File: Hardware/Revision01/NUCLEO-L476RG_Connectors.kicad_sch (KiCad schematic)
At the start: 29 parts, among them CN1 Header 19X2, CN2 Header 8X1_Female, CN3 Header 6X1_Female, CN4 Header 10X1_Female, CN5 Header 8X1_Female, CN6 Header 19X2

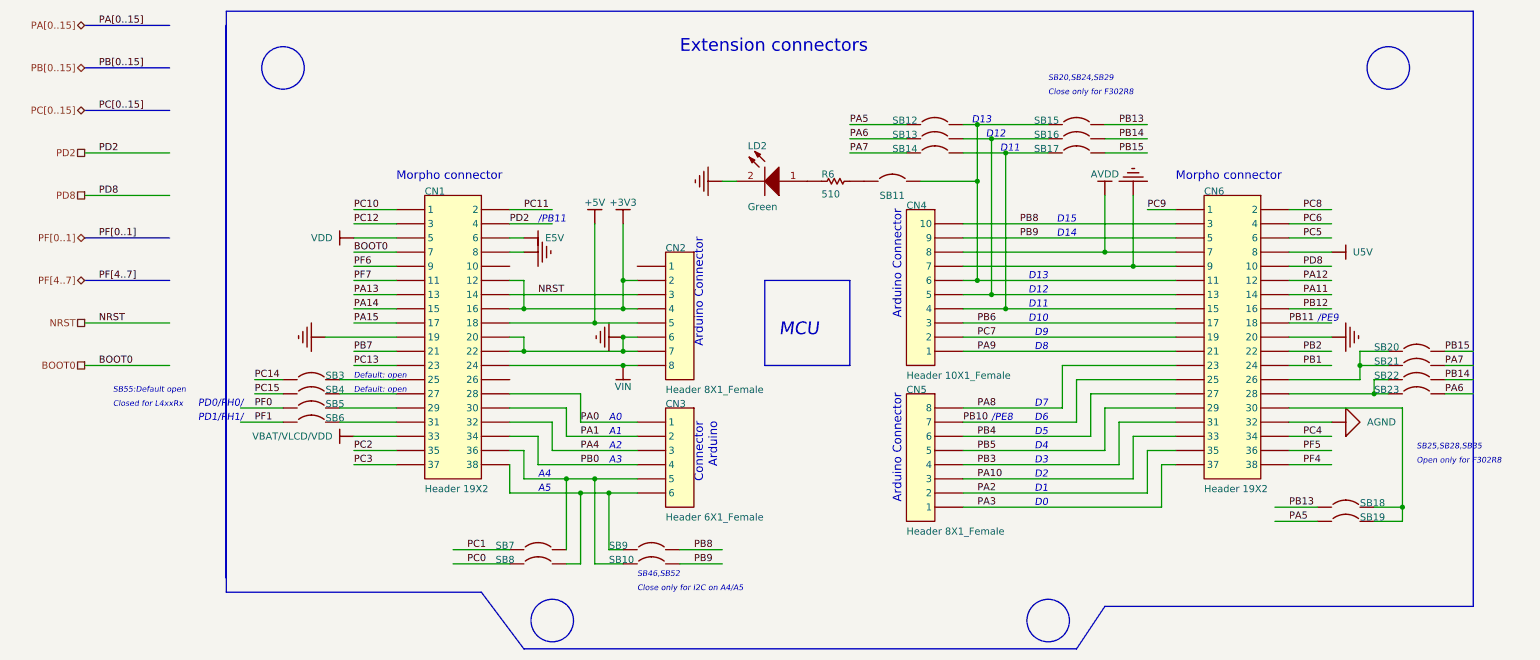
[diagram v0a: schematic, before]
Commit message: . Renamed schematic files, removed old symbol files
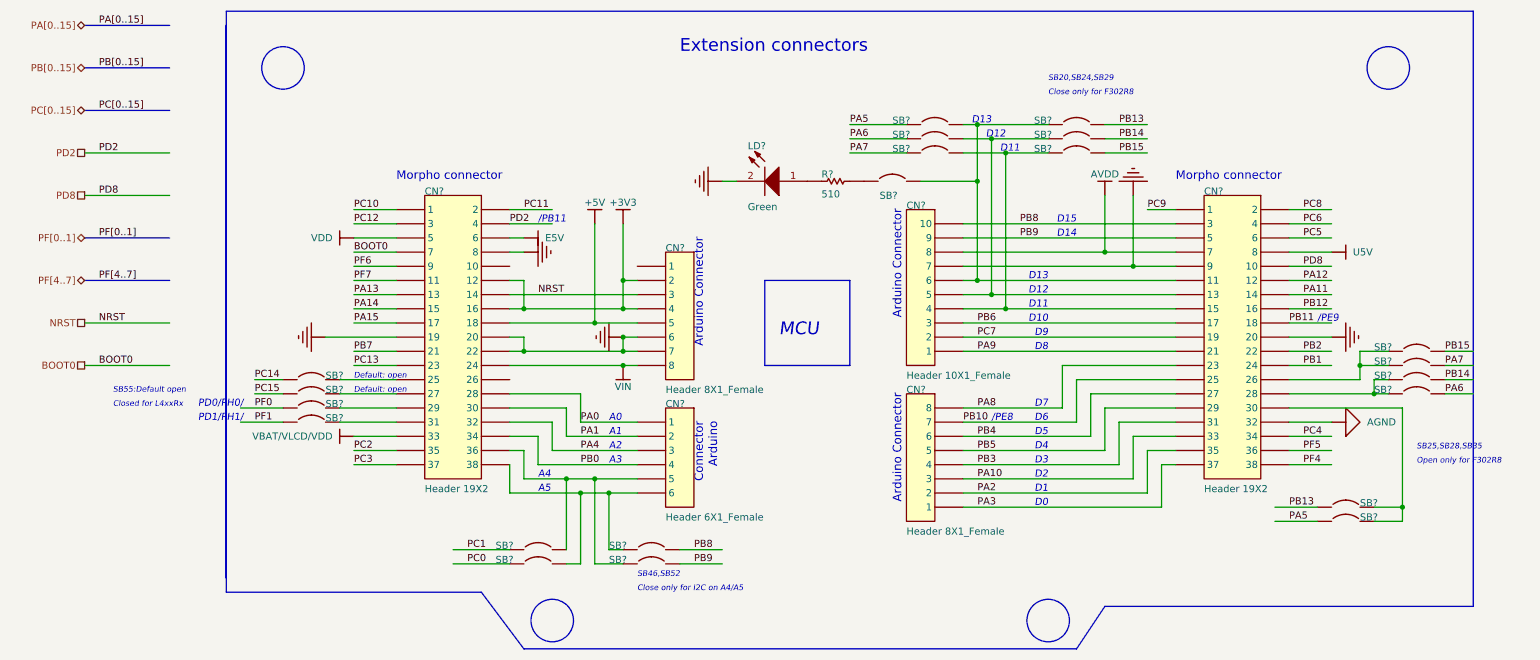
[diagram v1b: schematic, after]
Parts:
- renumbered CN4 to CN?, CN6 to CN?, CN5 to CN?, CN1 to CN?, CN3 to CN?, CN2 to CN?, LD2 to LD?, R6 to R?, SB21 to SB?, SB22 to SB?, SB16 to SB?, SB8 to SB?, SB20 to SB?, SB17 to SB?, SB5 to SB?, SB13 to SB?, SB14 to SB?, SB12 to SB?, SB4 to SB?, SB11 to SB?, SB15 to SB?, SB9 to SB?, SB10 to SB?, SB23 to SB?, SB18 to SB?, SB3 to SB?, SB19 to SB?, SB6 to SB?, SB7 to SB?

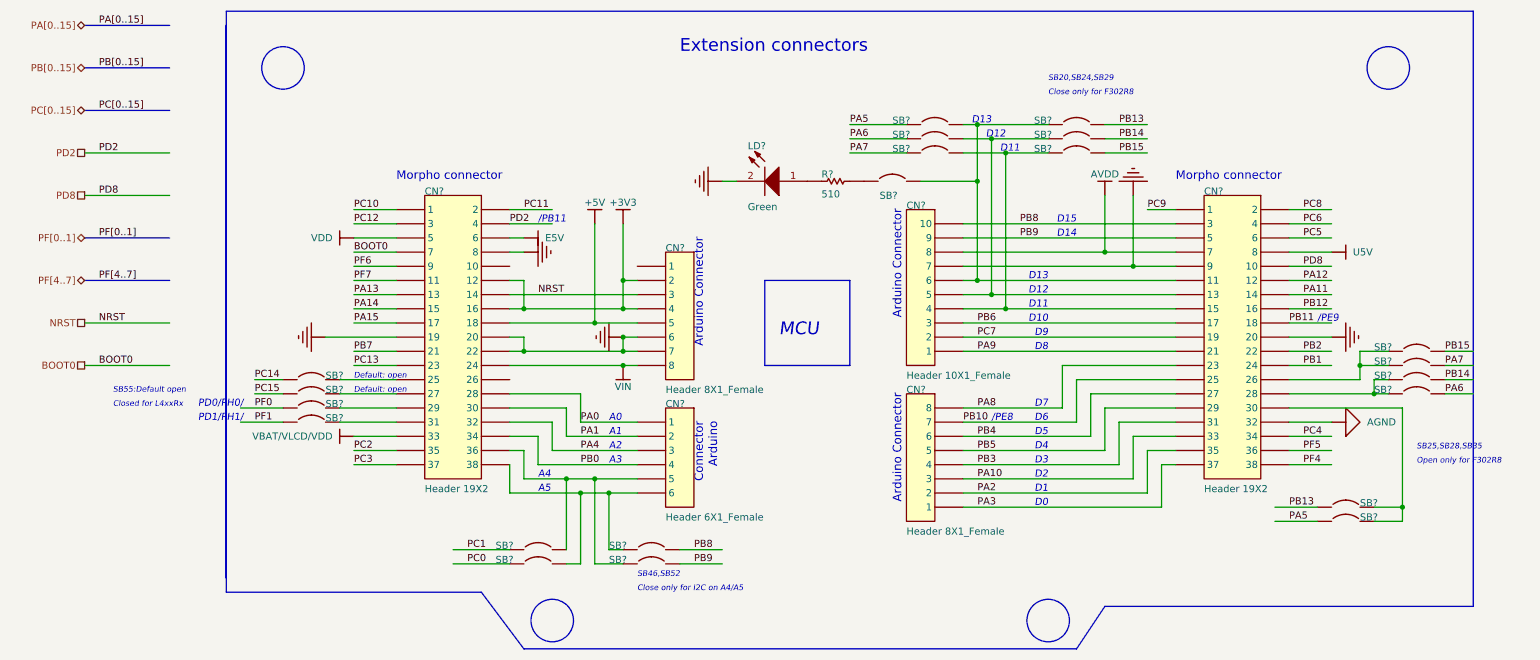
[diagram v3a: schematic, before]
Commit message: . Completed MCU schematic & imported hierarchical model pins
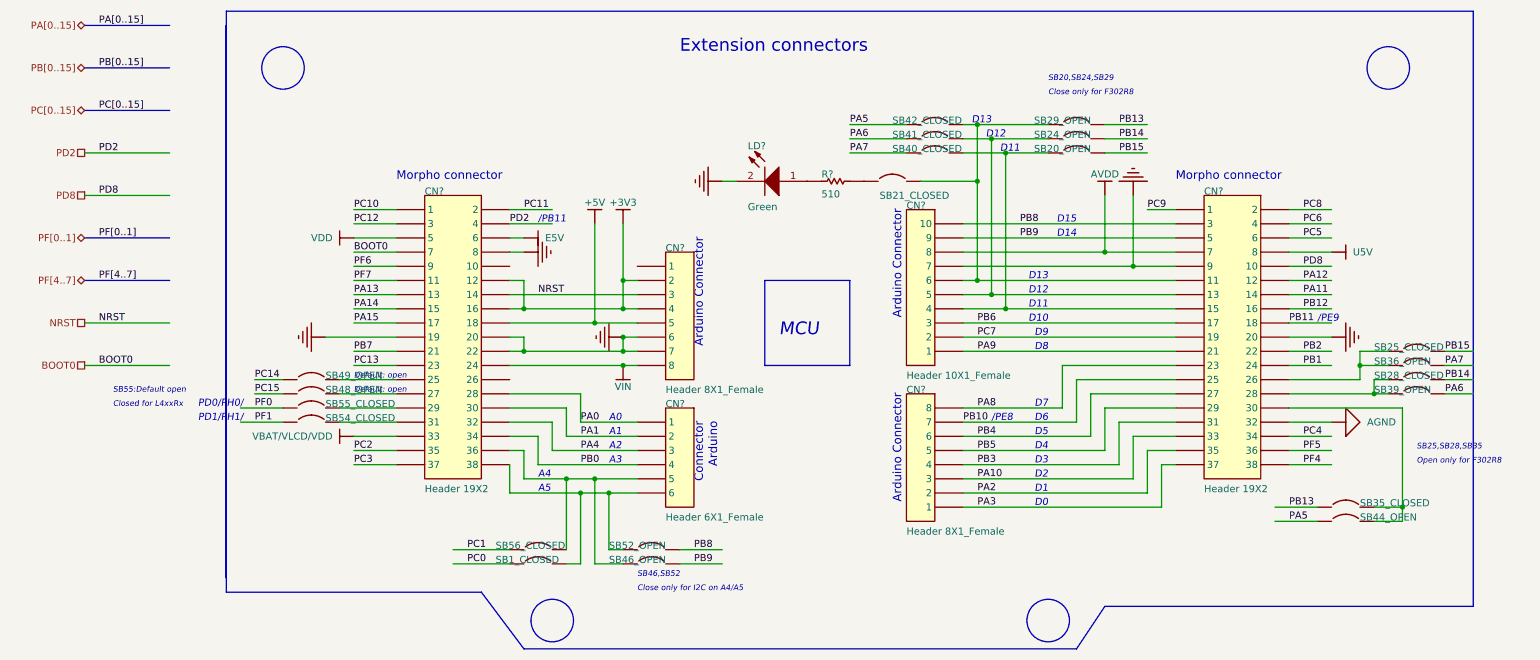
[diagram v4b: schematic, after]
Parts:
- gave numbers to parts that had none: 21
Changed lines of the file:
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@@
 		(on_board yes)
 		(dnp no)
-		(property "Reference" "SB?"
+		(property "Reference" "SB36_OPEN"
 			(at 257.81 95.25 0)
 			(effects
@@
 			(project "Revision01"
 				(path "/955cc99e-a129-42cf-abc7-aa99813fdb5f/00000000-0000-0000-0000-00005ea70ac3/dfd3e576-45ac-414e-879c-fe3a4e293d3a/d95c2c22-4412-4afc-9129-04f7fbe3da60"
-					(reference "SB?")
+					(reference "SB36_OPEN")
 					(unit 1)
 				)
@@
 		(on_board yes)
 		(dnp no)
-		(property "Reference" "SB?"
+		(property "Reference" "SB28_CLOSED"
 			(at 257.81 97.79 0)
 			(effects
@@
 			(project "Revision01"
 				(path "/955cc99e-a129-42cf-abc7-aa99813fdb5f/00000000-0000-0000-0000-00005ea70ac3/dfd3e576-45ac-414e-879c-fe3a4e293d3a/d95c2c22-4412-4afc-9129-04f7fbe3da60"
-					(reference "SB?")
+					(reference "SB28_CLOSED")
 					(unit 1)
 				)
@@
 		(on_board yes)
 		(dnp no)
-		(property "Reference" "SB?"
+		(property "Reference" "SB24_OPEN"
 			(at 196.85 54.61 0)
 			(effects
@@
 			(project "Revision01"
 				(path "/955cc99e-a129-42cf-abc7-aa99813fdb5f/00000000-0000-0000-0000-00005ea70ac3/dfd3e576-45ac-414e-879c-fe3a4e293d3a/d95c2c22-4412-4afc-9129-04f7fbe3da60"
-					(reference "SB?")
+					(reference "SB24_OPEN")
 					(unit 1)
 				)
@@
 		(on_board yes)
 		(dnp no)
-		(property "Reference" "SB?"
+		(property "Reference" "SB1_CLOSED"
 			(at 100.33 130.81 0)
 			(effects
@@
 			(project "Revision01"
 				(path "/955cc99e-a129-42cf-abc7-aa99813fdb5f/00000000-0000-0000-0000-00005ea70ac3/dfd3e576-45ac-414e-879c-fe3a4e293d3a/d95c2c22-4412-4afc-9129-04f7fbe3da60"
-					(reference "SB?")
+					(reference "SB1_CLOSED")
 					(unit 1)
 				)
@@
 		(on_board yes)
 		(dnp no)
-		(property "Reference" "SB?"
+		(property "Reference" "SB25_CLOSED"
 			(at 257.81 92.71 0)
 			(effects
@@
 			(project "Revision01"
 				(path "/955cc99e-a129-42cf-abc7-aa99813fdb5f/00000000-0000-0000-0000-00005ea70ac3/dfd3e576-45ac-414e-879c-fe3a4e293d3a/d95c2c22-4412-4afc-9129-04f7fbe3da60"
-					(reference "SB?")
+					(reference "SB25_CLOSED")
 					(unit 1)
 				)
@@
 		(on_board yes)
 		(dnp no)
-		(property "Reference" "SB?"
+		(property "Reference" "SB20_OPEN"
 			(at 196.85 57.15 0)
 			(effects
@@
 			(project "Revision01"
 				(path "/955cc99e-a129-42cf-abc7-aa99813fdb5f/00000000-0000-0000-0000-00005ea70ac3/dfd3e576-45ac-414e-879c-fe3a4e293d3a/d95c2c22-4412-4afc-9129-04f7fbe3da60"
-					(reference "SB?")
+					(reference "SB20_OPEN")
 					(unit 1)
 				)
@@
 		(on_board yes)
 		(dnp no)
-		(property "Reference" "SB?"
+		(property "Reference" "SB55_CLOSED"
 			(at 69.85 102.87 0)
 			(effects
@@
 			(project "Revision01"
 				(path "/955cc99e-a129-42cf-abc7-aa99813fdb5f/00000000-0000-0000-0000-00005ea70ac3/dfd3e576-45ac-414e-879c-fe3a4e293d3a/d95c2c22-4412-4afc-9129-04f7fbe3da60"
-					(reference "SB?")
+					(reference "SB55_CLOSED")
 					(unit 1)
 				)
@@
 		(on_board yes)
 		(dnp no)
-		(property "Reference" "SB?"
+		(property "Reference" "SB41_CLOSED"
 			(at 171.45 54.61 0)
 			(effects
@@
 			(project "Revision01"
 				(path "/955cc99e-a129-42cf-abc7-aa99813fdb5f/00000000-0000-0000-0000-00005ea70ac3/dfd3e576-45ac-414e-879c-fe3a4e293d3a/d95c2c22-4412-4afc-9129-04f7fbe3da60"
-					(reference "SB?")
+					(reference "SB41_CLOSED")
 					(unit 1)
 				)
@@
 		(on_board yes)
 		(dnp no)
-		(property "Reference" "SB?"
+		(property "Reference" "SB40_CLOSED"
 			(at 171.45 57.15 0)
 			(effects
@@
 			(project "Revision01"
 				(path "/955cc99e-a129-42cf-abc7-aa99813fdb5f/00000000-0000-0000-0000-00005ea70ac3/dfd3e576-45ac-414e-879c-fe3a4e293d3a/d95c2c22-4412-4afc-9129-04f7fbe3da60"
-					(reference "SB?")
+					(reference "SB40_CLOSED")
 					(unit 1)
 				)
@@
 		(on_board yes)
 		(dnp no)
-		(property "Reference" "SB?"
+		(property "Reference" "SB42_CLOSED"
 			(at 171.45 52.07 0)
 			(effects
@@
 			(project "Revision01"
 				(path "/955cc99e-a129-42cf-abc7-aa99813fdb5f/00000000-0000-0000-0000-00005ea70ac3/dfd3e576-45ac-414e-879c-fe3a4e293d3a/d95c2c22-4412-4afc-9129-04f7fbe3da60"
-					(reference "SB?")
+					(reference "SB42_CLOSED")
 					(unit 1)
 				)
@@
 		(on_board yes)
 		(dnp no)
-		(property "Reference" "SB?"
+		(property "Reference" "SB48_OPEN"
 			(at 69.85 100.33 0)
 			(effects
@@
 			(project "Revision01"
 				(path "/955cc99e-a129-42cf-abc7-aa99813fdb5f/00000000-0000-0000-0000-00005ea70ac3/dfd3e576-45ac-414e-879c-fe3a4e293d3a/d95c2c22-4412-4afc-9129-04f7fbe3da60"
-					(reference "SB?")
+					(reference "SB48_OPEN")
 					(unit 1)
 				)
@@
 		(on_board yes)
 		(dnp no)
-		(property "Reference" "SB?"
+		(property "Reference" "SB21_CLOSED"
 			(at 169.164 65.532 0)
 			(effects
@@
 			(project "Revision01"
 				(path "/955cc99e-a129-42cf-abc7-aa99813fdb5f/00000000-0000-0000-0000-00005ea70ac3/dfd3e576-45ac-414e-879c-fe3a4e293d3a/d95c2c22-4412-4afc-9129-04f7fbe3da60"
-					(reference "SB?")
+					(reference "SB21_CLOSED")
 					(unit 1)
 				)
@@
 		(on_board yes)
 		(dnp no)
-		(property "Reference" "SB?"
+		(property "Reference" "SB29_OPEN"
 			(at 196.85 52.07 0)
 			(effects
@@
 			(project "Revision01"
 				(path "/955cc99e-a129-42cf-abc7-aa99813fdb5f/00000000-0000-0000-0000-00005ea70ac3/dfd3e576-45ac-414e-879c-fe3a4e293d3a/d95c2c22-4412-4afc-9129-04f7fbe3da60"
-					(reference "SB?")
+					(reference "SB29_OPEN")
 					(unit 1)
 				)
@@
 		(on_board yes)
 		(dnp no)
-		(property "Reference" "SB?"
+		(property "Reference" "SB52_OPEN"
 			(at 120.65 128.27 0)
 			(effects
@@
 			(project "Revision01"
 				(path "/955cc99e-a129-42cf-abc7-aa99813fdb5f/00000000-0000-0000-0000-00005ea70ac3/dfd3e576-45ac-414e-879c-fe3a4e293d3a/d95c2c22-4412-4afc-9129-04f7fbe3da60"
-					(reference "SB?")
+					(reference "SB52_OPEN")
 					(unit 1)
 				)
@@
 		(on_board yes)
 		(dnp no)
-		(property "Reference" "SB?"
+		(property "Reference" "SB46_OPEN"
 			(at 120.65 130.81 0)
 			(effects
@@
 			(project "Revision01"
 				(path "/955cc99e-a129-42cf-abc7-aa99813fdb5f/00000000-0000-0000-0000-00005ea70ac3/dfd3e576-45ac-414e-879c-fe3a4e293d3a/d95c2c22-4412-4afc-9129-04f7fbe3da60"
-					(reference "SB?")
+					(reference "SB46_OPEN")
 					(unit 1)
 				)
@@
 		(on_board yes)
 		(dnp no)
-		(property "Reference" "SB?"
+		(property "Reference" "SB39_OPEN"
 			(at 257.81 100.33 0)
 			(effects
@@
 			(project "Revision01"
 				(path "/955cc99e-a129-42cf-abc7-aa99813fdb5f/00000000-0000-0000-0000-00005ea70ac3/dfd3e576-45ac-414e-879c-fe3a4e293d3a/d95c2c22-4412-4afc-9129-04f7fbe3da60"
-					(reference "SB?")
+					(reference "SB39_OPEN")
 					(unit 1)
 				)
@@
 		(on_board yes)
 		(dnp no)
-		(property "Reference" "SB?"
+		(property "Reference" "SB35_CLOSED"
 			(at 255.27 120.65 0)
 			(effects
@@
 			(project "Revision01"
 				(path "/955cc99e-a129-42cf-abc7-aa99813fdb5f/00000000-0000-0000-0000-00005ea70ac3/dfd3e576-45ac-414e-879c-fe3a4e293d3a/d95c2c22-4412-4afc-9129-04f7fbe3da60"
-					(reference "SB?")
+					(reference "SB35_CLOSED")
 					(unit 1)
 				)
@@
 		(on_board yes)
 		(dnp no)
-		(property "Reference" "SB?"
+		(property "Reference" "SB49_OPEN"
 			(at 69.85 97.79 0)
 			(effects
@@
 			(project "Revision01"
 				(path "/955cc99e-a129-42cf-abc7-aa99813fdb5f/00000000-0000-0000-0000-00005ea70ac3/dfd3e576-45ac-414e-879c-fe3a4e293d3a/d95c2c22-4412-4afc-9129-04f7fbe3da60"
-					(reference "SB?")
+					(reference "SB49_OPEN")
 					(unit 1)
 				)
@@
 		(on_board yes)
 		(dnp no)
-		(property "Reference" "SB?"
+		(property "Reference" "SB44_OPEN"
 			(at 255.27 123.19 0)
 			(effects
@@
 			(project "Revision01"
 				(path "/955cc99e-a129-42cf-abc7-aa99813fdb5f/00000000-0000-0000-0000-00005ea70ac3/dfd3e576-45ac-414e-879c-fe3a4e293d3a/d95c2c22-4412-4afc-9129-04f7fbe3da60"
-					(reference "SB?")
+					(reference "SB44_OPEN")
 					(unit 1)
 				)
@@
 		(on_board yes)
 		(dnp no)
-		(property "Reference" "SB?"
+		(property "Reference" "SB54_CLOSED"
 			(at 69.85 105.41 0)
 			(effects
@@
 			(project "Revision01"
 				(path "/955cc99e-a129-42cf-abc7-aa99813fdb5f/00000000-0000-0000-0000-00005ea70ac3/dfd3e576-45ac-414e-879c-fe3a4e293d3a/d95c2c22-4412-4afc-9129-04f7fbe3da60"
-					(reference "SB?")
+					(reference "SB54_CLOSED")
 					(unit 1)
 				)
@@
 		(on_board yes)
 		(dnp no)
-		(property "Reference" "SB?"
+		(property "Reference" "SB56_CLOSED"
 			(at 100.33 128.27 0)
 			(effects
@@
 			(project "Revision01"
 				(path "/955cc99e-a129-42cf-abc7-aa99813fdb5f/00000000-0000-0000-0000-00005ea70ac3/dfd3e576-45ac-414e-879c-fe3a4e293d3a/d95c2c22-4412-4afc-9129-04f7fbe3da60"
-					(reference "SB?")
+					(reference "SB56_CLOSED")
 					(unit 1)
 				)

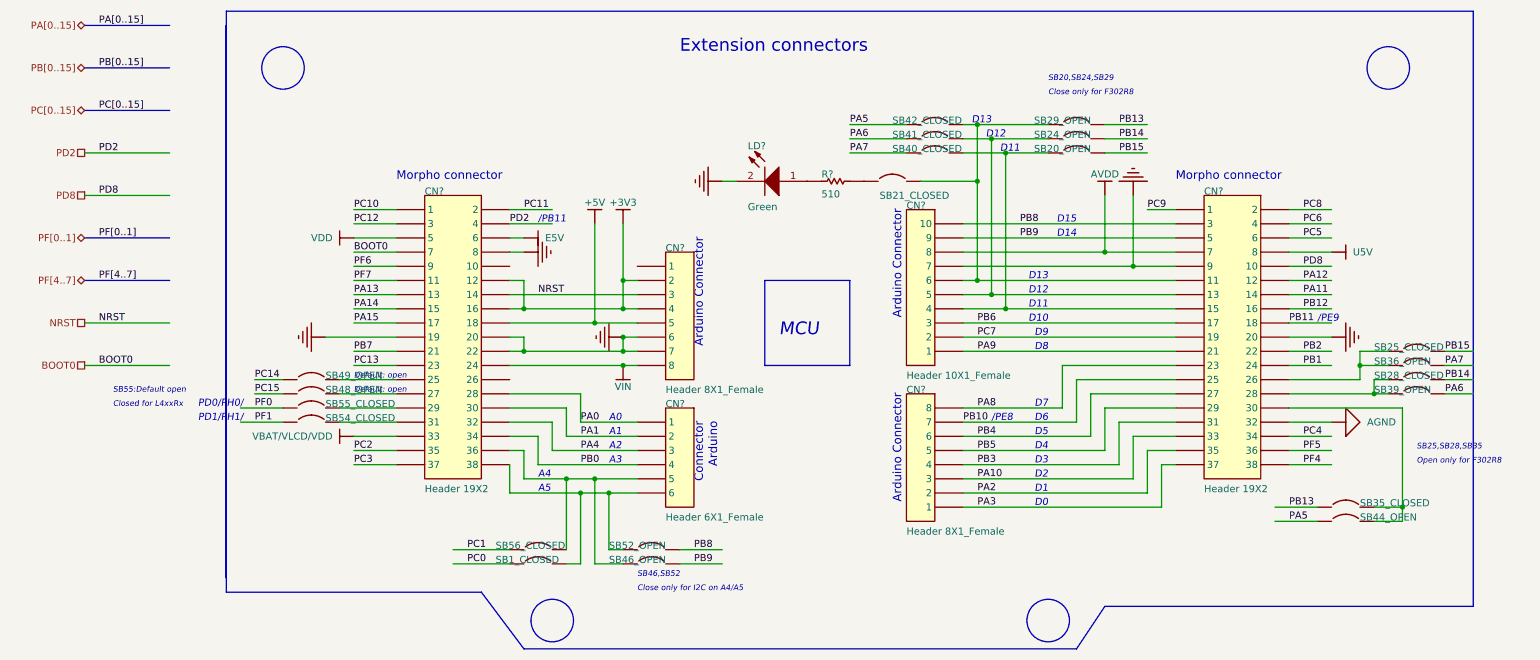
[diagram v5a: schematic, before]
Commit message: CREATE STM32CUBEIDE file to verify all ports Check over CONTROLLER SHEET Improve annotation ordering Move testpoints out of controller sheet
Still performering ERC check
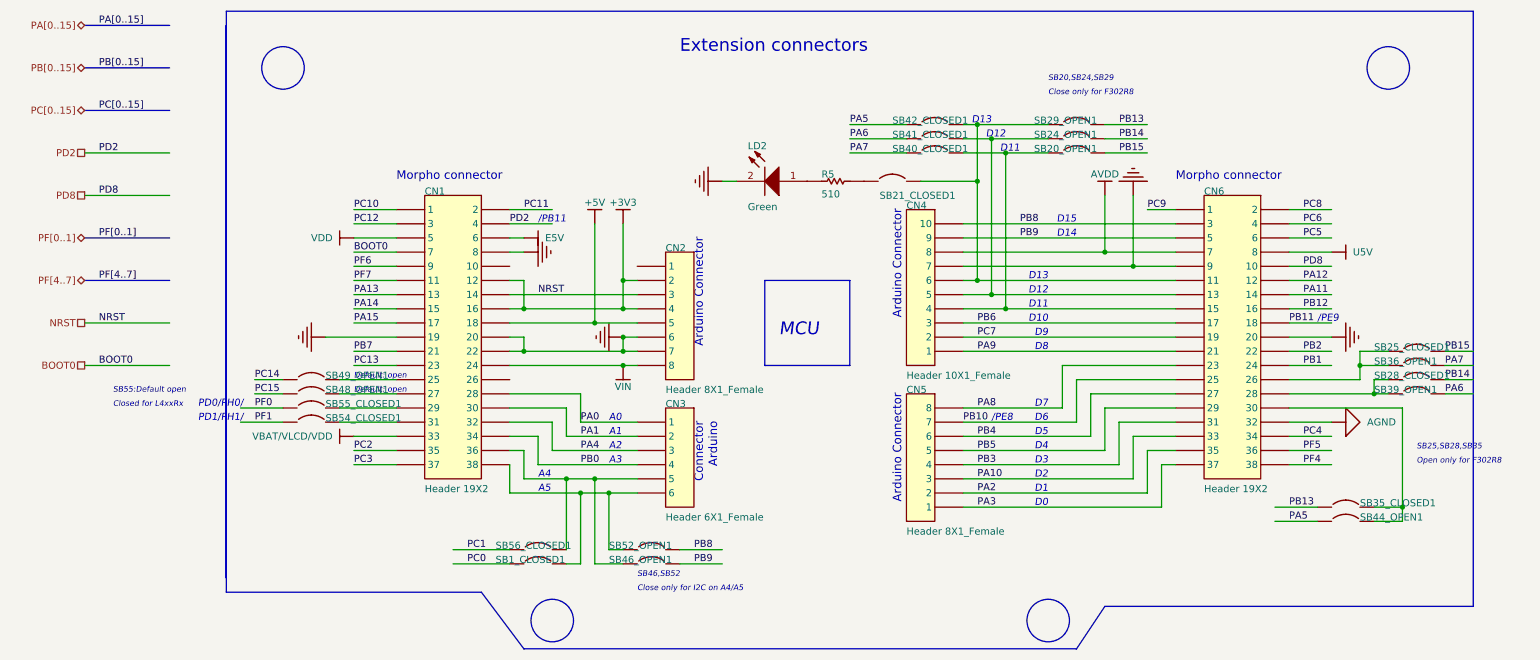
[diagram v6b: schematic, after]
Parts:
- gave numbers to parts that had none: 8
- renumbered SB1_CLOSED to SB1_CLOSED1, SB20_OPEN to SB20_OPEN1, SB21_CLOSED to SB21_CLOSED1, SB24_OPEN to SB24_OPEN1, SB25_CLOSED to SB25_CLOSED1, SB28_CLOSED to SB28_CLOSED1, SB29_OPEN to SB29_OPEN1, SB35_CLOSED to SB35_CLOSED1, SB36_OPEN to SB36_OPEN1, SB39_OPEN to SB39_OPEN1, SB40_CLOSED to SB40_CLOSED1, SB41_CLOSED to SB41_CLOSED1, SB42_CLOSED to SB42_CLOSED1, SB44_OPEN to SB44_OPEN1, SB46_OPEN to SB46_OPEN1, SB48_OPEN to SB48_OPEN1, SB49_OPEN to SB49_OPEN1, SB52_OPEN to SB52_OPEN1, SB54_CLOSED to SB54_CLOSED1, SB55_CLOSED to SB55_CLOSED1, SB56_CLOSED to SB56_CLOSED1
